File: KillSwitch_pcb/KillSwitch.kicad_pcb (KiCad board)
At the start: 2 copper layers, 97.8 x 69.8 mm, 82 parts, among them IC1 Wio-SX1262, J1 J_ESP_DBG_UART, J2 USB_C_Receptacle_USB2.0, SW1 SW_DIP_x08, SW2 SW_RESET, SW4 ARM, SW5 KILL1, SW6 KILL2, SW7 KILL3, SW8 KILL4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

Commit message: końcowa werjsa
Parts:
- added D19: Amber, LED_THT:LED_Rectangular_W5.0mm_H2.0mm, F.Cu at (145.6, 93.8)
- added R27: 120R, Resistor_SMD:R_0805_2012Metric_Pad1.20x1.40mm_HandSolder, F.Cu at (148.1, 92.0)
- moved H1 59.6 mm to (83.0, 89.8)
- moved SW4 30.0 mm to (137.3, 91.9), turned to 180 degrees
- moved H3 24.2 mm to (132.6, 110.0)
- moved H4 23.4 mm to (215.4, 110.0)
- renumbered BOOT to SW3
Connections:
- U1 pad 25: unconnected-(U1-IO48-Pad25) -> /LED_ARM
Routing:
- net /LED_ARM: track 0.00 -> 27.2 mm, vias 0 -> 2
- net GND: track 141.7 -> 161.1 mm, vias 78 -> 63
- net (no net): track 41.5 -> 27.3 mm, vias 2 -> 0
- net /SW_ARM: track 36.6 -> 30.9 mm
- net Net-(D19-K): track 0.00 -> 3.81 mm
- net /ESP_USB2_N: track 22.8 -> 25.0 mm
- net /ESP_USB2_P: track 22.8 -> 25.0 mm
- net Net-(J2-CC2): track 10.3 -> 9.45 mm
- net /KillSwitchIO/SCK: track 54.8 -> 54.2 mm
- net /+3.3v_ESP: track 157.6 -> 157.0 mm
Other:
- board size 97.8 x 69.8 mm -> 91.4 x 69.8 mm

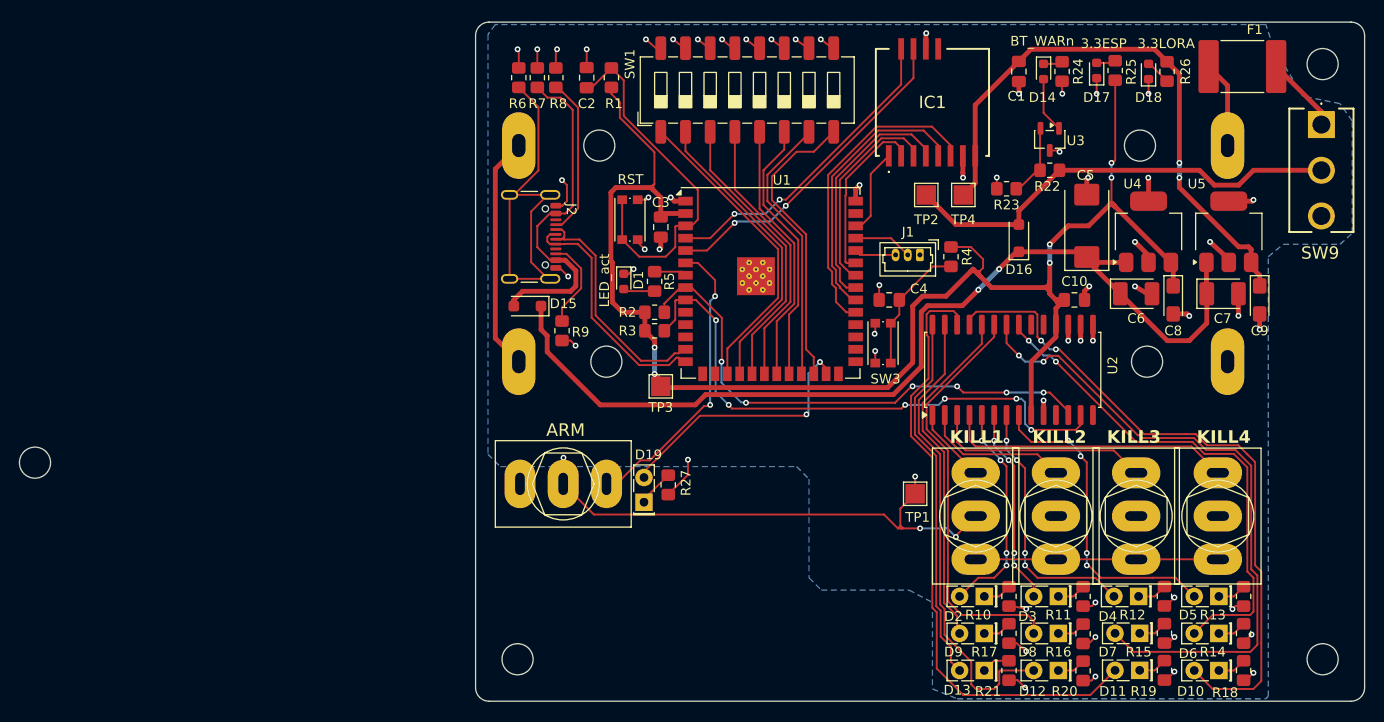
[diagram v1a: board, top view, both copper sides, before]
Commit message: Move LEDs resistors to the back side, correct decoupling caps, add aesthetic changes
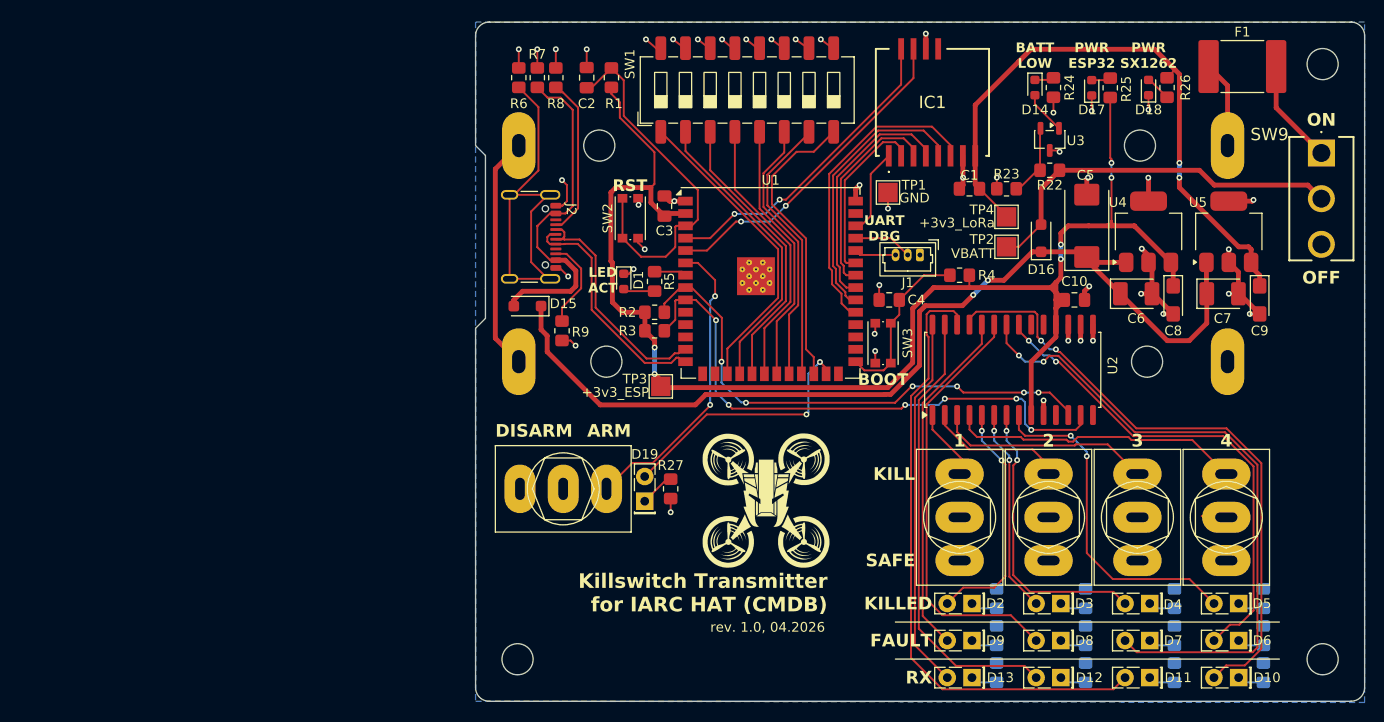
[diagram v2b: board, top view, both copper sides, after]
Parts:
- removed H4: MountingHole, MountingHole:MountingHole_3.2mm_M3_DIN965
- R10, R11, R12, R13, R14, R15, R16, R17, R18, R19, R20, R21: moved to B.Cu
- moved H1 138.6 mm to (215.4, 48.8)
- moved H2 61.2 mm to (215.4, 110.0)
- moved TP1 31.1 mm to (170.7, 62.0)
- moved C1 13.1 mm to (179.1, 61.6), turned to 0 degrees
- moved TP2 9.83 mm to (182.9, 67.6)
- moved TP4 4.98 mm to (182.9, 64.5)
- moved SW9 2.92 mm to (215.3, 57.9)
- moved D16 2.29 mm to (186.4, 66.7)
- moved C3 2.19 mm to (147.7, 63.4), turned to -90 degrees
- moved D5 2.16 mm to (206.8, 104.3)
- moved D6 2.16 mm to (206.8, 108.1)
- moved D10 2.16 mm to (206.8, 111.9)
- moved R4 2.10 mm to (178.1, 70.5), turned to 180 degrees
- moved R13 2.05 mm to (209.3, 103.7), turned to 90 degrees
- moved R14 2.05 mm to (209.3, 107.6), turned to 90 degrees
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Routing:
- net GND: track 161.1 -> 92.5 mm, vias 63 -> 46
- net (no net): track 27.3 -> 2.40 mm
- net /KillSwitchPower/+VBATT: track 46.3 -> 39.0 mm
- net /+3.3v_ESP: track 157.0 -> 150.2 mm
- net /KillSwitchIO/LED_RX1: track 68.9 -> 63.9 mm
- net /+3.3v_LoRa: track 60.3 -> 64.2 mm
- net /BOOT_MODE: track 13.6 -> 17.4 mm
- net /KillSwitchIO/LED_KILLED3: track 26.7 -> 29.8 mm, vias 4 -> 2
- net Net-(SW9-A): track 7.90 -> 10.8 mm
- net /KillSwitchIO/LED_KILLED1: track 22.7 -> 24.7 mm, vias 4 -> 2
- net /KillSwitchIO/LED_RX3: track 48.5 -> 46.5 mm
- net /KillSwitchIO/LED_KILLED4: track 33.2 -> 35.1 mm, vias 4 -> 2
- net /KillSwitchIO/LED_FAULT1: track 52.1 -> 50.7 mm
- net /KillSwitchPower/BATT_WARNING: track 5.72 -> 4.43 mm
- net /KillSwitchIO/LED_RX2: track 63.3 -> 64.5 mm
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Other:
- outline, holes or cut-outs redrawn
- board text added: "+3v3_ESP"
- board text added: "+3v3_LoRa"
- board text added: "1"
- board text added: "2"
- board text added: "3"
- board text added: "4"
- board text added: "BATT LOW"
- board text added: "BOOT"
- board text added: "DISARM"
- board text added: "FAULT"
- board text added: "GND"
- board text added: "KILL"
- board text added: "KILLED"
- board text added: "Killswitch Transmitter for IARC HAT (CMDB)"
- board text added: "LED ACT"
- board text added: "Notes:"
- board text added: "OFF"
- board text added: "ON"
- board text added: "PWR ESP32"
- board text added: "PWR SX1262"
- board text added: "RX"
- board text added: "SAFE"
- board text added: "UART DBG"
- board text added: "VBATT"
- board text added: "rev. 1.0, 04.2026"
- board text removed: "3.3ESP"
- board text removed: "3.3LORA"
- board text removed: "BT_WARn"
- board text removed: "KILL1"
- board text removed: "KILL2"
- board text removed: "KILL3"
- board text removed: "KILL4"
- board text removed: "LED_act"
